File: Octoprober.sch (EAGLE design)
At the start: 135 parts, among them J1 10118193-0001LF, J2 26-60-4020, P1 TC33X-1, SW1 101-0134-EV, SW2 EVQ-Q2203W, SW3 EVQ-Q2203W, SW4 EVQ-Q2203W, SW5 EVQ-Q2203W, U1 P8X32A-M44, U10 MAX31855KASA+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

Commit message: Finished REV0.
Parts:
- BATT1: value 1042 -> (none); device PP_Connectors:LI-ION_18650_HOLDER1042 -> PP_Connectors:PH_1X02HEADER_PTH
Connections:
- net GND: now also BATT1.1; no longer BATT1.-
- net VBATT: now also BATT1.2; no longer BATT1.+
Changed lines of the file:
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@@
 <part name="C29" library="PP_Passives" deviceset="CAPACITOR_NON_POLAR" device="0402" value="0.1uF"/>
 <part name="C30" library="PP_Passives" deviceset="CAPACITOR_NON_POLAR" device="0402" value="0.01uF"/>
-<part name="BATT1" library="PP_Connectors" deviceset="LI-ION_18650_HOLDER" device="1042" value="1042"/>
 <part name="U5" library="PP_PowerIC" deviceset="BQ2407X" device="QFN-16" value="BQ24075RGTT"/>
 <part name="R14" library="PP_Passives" deviceset="RESISTOR" device="0402" value="10K"/>
@@
 <part name="D10" library="PP_Passives" deviceset="TVS_DIODE_DUAL" device="SOT-23" value="NUP2105LT1G"/>
 <part name="D11" library="PP_Passives" deviceset="TVS_DIODE_DUAL" device="SOT-23" value="NUP2105LT1G"/>
+<part name="BATT1" library="PP_Connectors" deviceset="PH_1X02" device="HEADER_PTH"/>
 </parts>
 <sheets>
@@
 <instance part="C29" gate="G$1" x="-223.52" y="-66.04"/>
 <instance part="C30" gate="G$1" x="-215.9" y="-66.04"/>
-<instance part="BATT1" gate="G$1" x="165.1" y="-12.7" rot="R90"/>
 <instance part="U5" gate="G$1" x="132.08" y="-2.54"/>
 <instance part="R14" gate="G$1" x="154.94" y="-17.78" rot="R270"/>
@@
 <instance part="D10" gate="G$1" x="-248.92" y="-50.8" rot="R270"/>
 <instance part="D11" gate="G$1" x="-248.92" y="-76.2" rot="R270"/>
+<instance part="BATT1" gate="G$1" x="162.56" y="-15.24" rot="R180"/>
 </instances>
 <busses>
@@
 </segment>
 <segment>
-<pinref part="BATT1" gate="G$1" pin="-"/>
-<wire x1="165.1" y1="-17.78" x2="165.1" y2="-33.02" width="0.1524" layer="91"/>
+<wire x1="165.1" y1="-15.24" x2="165.1" y2="-33.02" width="0.1524" layer="91"/>
 <pinref part="R14" gate="G$1" pin="2"/>
 <wire x1="154.94" y1="-22.86" x2="154.94" y2="-27.94" width="0.1524" layer="91"/>
@@
 <junction x="154.94" y="-27.94"/>
 <junction x="154.94" y="-33.02"/>
+<pinref part="BATT1" gate="G$1" pin="1"/>
+<wire x1="165.1" y1="-15.24" x2="162.56" y2="-15.24" width="0.1524" layer="91"/>
 </segment>
 <segment>
@@
 <net name="VBATT" class="0">
 <segment>
-<pinref part="BATT1" gate="G$1" pin="+"/>
-<wire x1="165.1" y1="-7.62" x2="165.1" y2="-2.54" width="0.1524" layer="91"/>
 <label x="152.4" y="-2.54" size="0.8128" layer="95" font="vector"/>
 <pinref part="U5" gate="G$1" pin="BAT"/>
@@
 <wire x1="172.72" y1="-2.54" x2="165.1" y2="-2.54" width="0.1524" layer="91"/>
 <junction x="165.1" y="-2.54"/>
-</segment>
-</net>
+<wire x1="165.1" y1="-2.54" x2="165.1" y2="-12.7" width="0.1524" layer="91"/>
+<pinref part="BATT1" gate="G$1" pin="2"/>
+<wire x1="165.1" y1="-12.7" x2="162.56" y2="-12.7" width="0.1524" layer="91"/>
+</segment>
+</net>

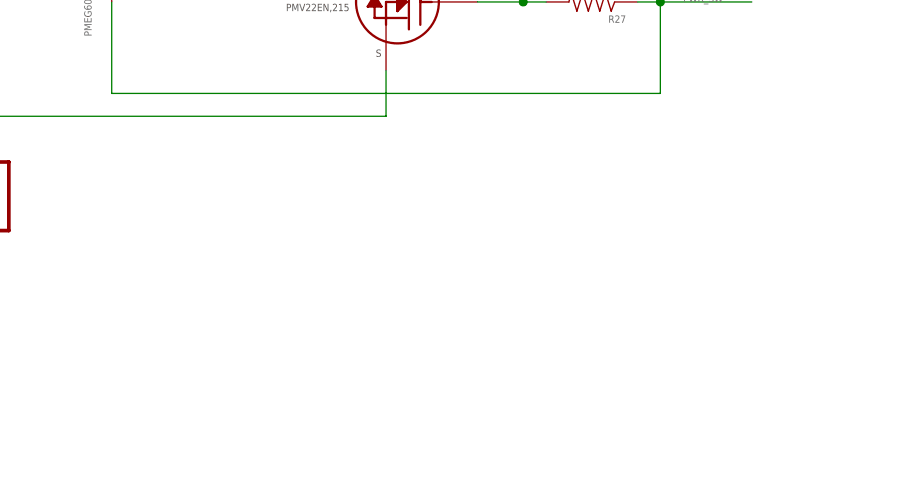
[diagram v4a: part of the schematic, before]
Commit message: Added ADC MCP3021 to monitor battery
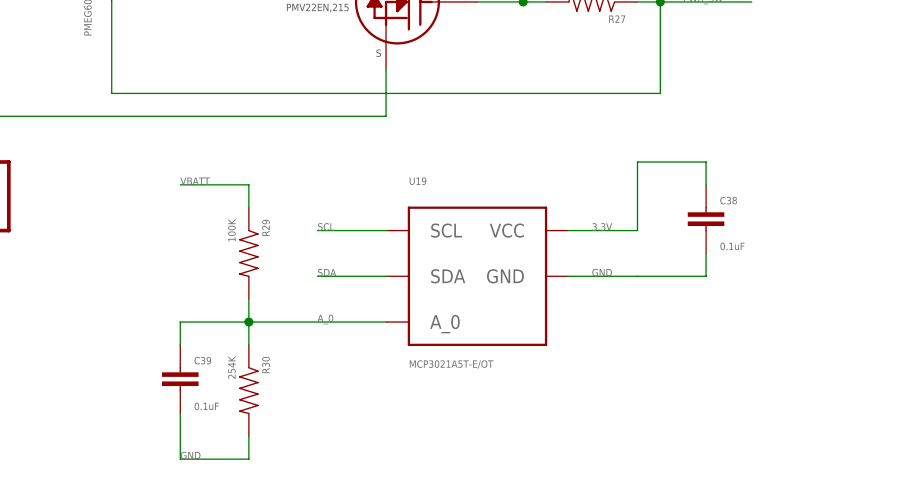
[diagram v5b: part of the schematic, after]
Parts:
- added C38, C39: 0.1uF, PP_Passives:CAPACITOR_NON_POLAR0402
- added R29: 100K, PP_Passives:RESISTOR0402
- added R30: 254K, PP_Passives:RESISTOR0402
- added U19: MCP3021A5T-E/OT, PP_DigitalIC:MCP3021SOT-23A
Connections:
- new net A_0: C39.1, R29.2, R30.1, U19.A_0
- net 3.3V: now also C38.1, U19.VCC
- net GND: now also C38.2, C39.2, R30.2, U19.GND
- net SCL: now also U19.SCL
- net SDA: now also U19.SDA
- net VBATT: now also R29.1
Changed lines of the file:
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@@
 <?xml version="1.0" encoding="utf-8"?>
 <!DOCTYPE eagle SYSTEM "eagle.dtd">
-<eagle version="6.5.0">
+<eagle version="6.3">
 <drawing>
 <settings>
@@
 <part name="D11" library="PP_Passives" deviceset="TVS_DIODE_DUAL" device="SOT-23" value="NUP2105LT1G"/>
 <part name="BATT1" library="PP_Connectors" deviceset="PH_1X02" device="HEADER_PTH"/>
+<part name="C38" library="PP_Passives" deviceset="CAPACITOR_NON_POLAR" device="0402" value="0.1uF"/>
+<part name="R29" library="PP_Passives" deviceset="RESISTOR" device="0402" value="100K"/>
+<part name="R30" library="PP_Passives" deviceset="RESISTOR" device="0402" value="254K"/>
+<part name="C39" library="PP_Passives" deviceset="CAPACITOR_NON_POLAR" device="0402" value="0.1uF"/>
+<part name="U19" library="PP_DigitalIC" deviceset="MCP3021" device="SOT-23A" value="MCP3021A5T-E/OT"/>
 </parts>
 <sheets>
@@
 <instance part="D11" gate="G$1" x="-248.92" y="-76.2" rot="R270"/>
 <instance part="BATT1" gate="G$1" x="162.56" y="-15.24" rot="R180"/>
+<instance part="C38" gate="G$1" x="144.78" y="-99.06"/>
+<instance part="R29" gate="G$1" x="93.98" y="-104.14" rot="R270"/>
+<instance part="R30" gate="G$1" x="93.98" y="-119.38" rot="R270"/>
+<instance part="C39" gate="G$1" x="86.36" y="-116.84"/>
+<instance part="U19" gate="G$1" x="119.38" y="-109.22"/>
 </instances>
 <busses>
@@
 <label x="-111.76" y="-119.38" size="0.8128" layer="95" font="vector"/>
 </segment>
+<segment>
+<wire x1="101.6" y1="-106.68" x2="109.22" y2="-106.68" width="0.1524" layer="91"/>
+<label x="101.6" y="-106.68" size="0.8128" layer="95" font="vector"/>
+<pinref part="U19" gate="G$1" pin="SDA"/>
+</segment>
 </net>
 <net name="SCL" class="0">
@@
 <wire x1="-104.14" y1="-114.3" x2="-114.3" y2="-114.3" width="0.1524" layer="91"/>
 <label x="-111.76" y="-114.3" size="0.8128" layer="95" font="vector"/>
+</segment>
+<segment>
+<wire x1="109.22" y1="-101.6" x2="101.6" y2="-101.6" width="0.1524" layer="91"/>
+<label x="101.6" y="-101.6" size="0.8128" layer="95" font="vector"/>
+<pinref part="U19" gate="G$1" pin="SCL"/>
 </segment>
 </net>
@@
 <pinref part="C37" gate="G$1" pin="2"/>
 <wire x1="-121.92" y1="-109.22" x2="-121.92" y2="-106.68" width="0.1524" layer="91"/>
+</segment>
+<segment>
+<wire x1="129.54" y1="-106.68" x2="137.16" y2="-106.68" width="0.1524" layer="91"/>
+<pinref part="C38" gate="G$1" pin="2"/>
+<wire x1="137.16" y1="-106.68" x2="144.78" y2="-106.68" width="0.1524" layer="91"/>
+<wire x1="144.78" y1="-106.68" x2="144.78" y2="-104.14" width="0.1524" layer="91"/>
+<label x="132.08" y="-106.68" size="0.8128" layer="95" font="vector"/>
+<pinref part="U19" gate="G$1" pin="GND"/>
+</segment>
+<segment>
+<pinref part="R30" gate="G$1" pin="2"/>
+<wire x1="93.98" y1="-124.46" x2="93.98" y2="-127" width="0.1524" layer="91"/>
+<wire x1="93.98" y1="-127" x2="86.36" y2="-127" width="0.1524" layer="91"/>
+<label x="86.36" y="-127" size="0.8128" layer="95" font="vector"/>
+<pinref part="C39" gate="G$1" pin="2"/>
+<wire x1="86.36" y1="-121.92" x2="86.36" y2="-127" width="0.1524" layer="91"/>
 </segment>
 </net>
@@
 <wire x1="-121.92" y1="-96.52" x2="-121.92" y2="-99.06" width="0.1524" layer="91"/>
 </segment>
+<segment>
+<wire x1="137.16" y1="-101.6" x2="129.54" y2="-101.6" width="0.1524" layer="91"/>
+<wire x1="137.16" y1="-101.6" x2="137.16" y2="-93.98" width="0.1524" layer="91"/>
+<pinref part="C38" gate="G$1" pin="1"/>
+<wire x1="137.16" y1="-93.98" x2="144.78" y2="-93.98" width="0.1524" layer="91"/>
+<wire x1="144.78" y1="-93.98" x2="144.78" y2="-96.52" width="0.1524" layer="91"/>
+<label x="132.08" y="-101.6" size="0.8128" layer="95" font="vector"/>
+<pinref part="U19" gate="G$1" pin="VCC"/>
+</segment>
 </net>
 <net name="SD_RW" class="0">
@@
 <pinref part="BATT1" gate="G$1" pin="2"/>
 <wire x1="165.1" y1="-12.7" x2="162.56" y2="-12.7" width="0.1524" layer="91"/>
+</segment>
+<segment>
+<pinref part="R29" gate="G$1" pin="1"/>
+<wire x1="93.98" y1="-99.06" x2="93.98" y2="-96.52" width="0.1524" layer="91"/>
+<wire x1="93.98" y1="-96.52" x2="86.36" y2="-96.52" width="0.1524" layer="91"/>
+<label x="86.36" y="-96.52" size="0.8128" layer="95" font="vector"/>
 </segment>
 </net>
@@
 </segment>
 </net>
+<net name="A_0" class="0">
+<segment>
+<pinref part="R29" gate="G$1" pin="2"/>
+<wire x1="109.22" y1="-111.76" x2="93.98" y2="-111.76" width="0.1524" layer="91"/>
+<wire x1="93.98" y1="-111.76" x2="93.98" y2="-109.22" width="0.1524" layer="91"/>
+<pinref part="R30" gate="G$1" pin="1"/>
+<wire x1="93.98" y1="-111.76" x2="93.98" y2="-114.3" width="0.1524" layer="91"/>
+<junction x="93.98" y="-111.76"/>
+<label x="101.6" y="-111.76" size="0.8128" layer="95" font="vector"/>
+<pinref part="C39" gate="G$1" pin="1"/>
+<wire x1="93.98" y1="-111.76" x2="86.36" y2="-111.76" width="0.1524" layer="91"/>
+<wire x1="86.36" y1="-111.76" x2="86.36" y2="-114.3" width="0.1524" layer="91"/>
+<pinref part="U19" gate="G$1" pin="A_0"/>
+</segment>
+</net>

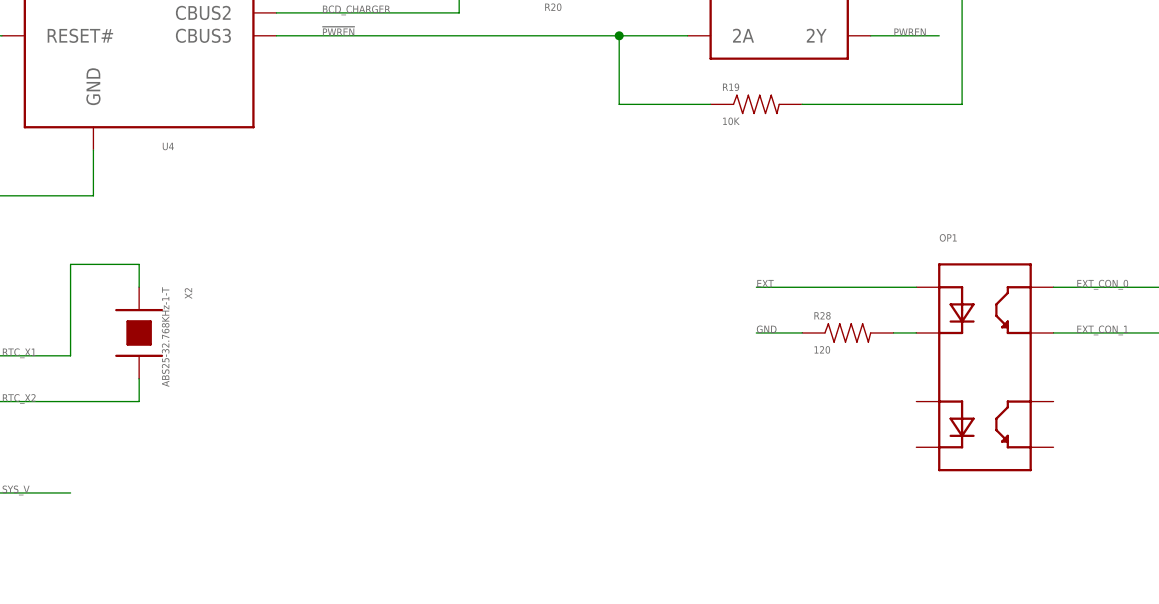
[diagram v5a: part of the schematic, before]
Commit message: Added part values and created BOM.txt
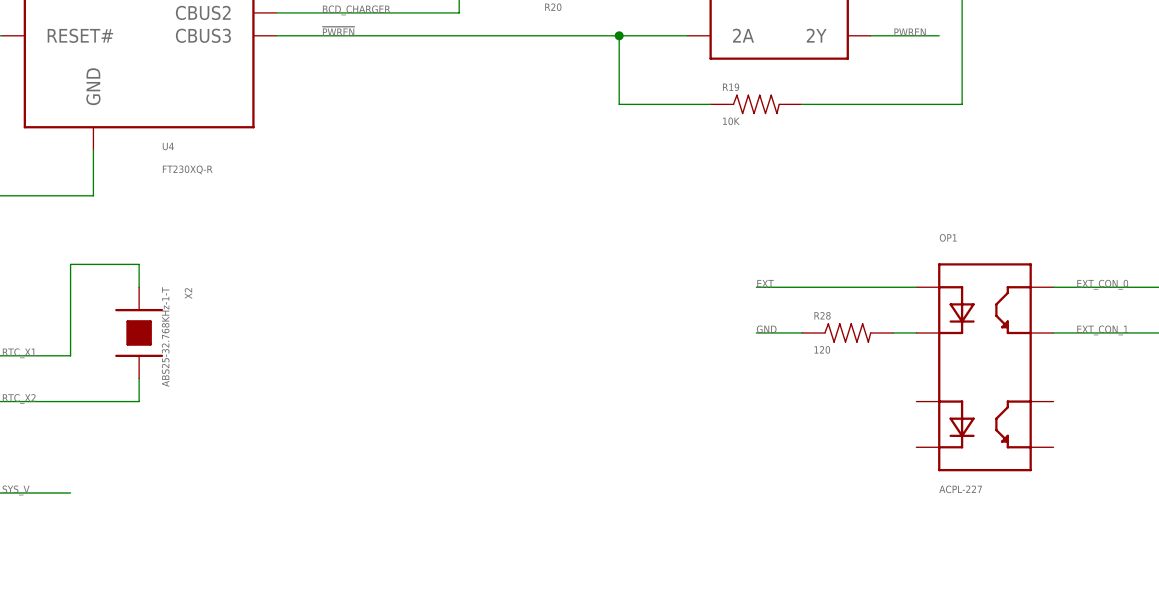
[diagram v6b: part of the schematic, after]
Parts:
- OP1: value (none) -> ACPL-227
- U4: value (none) -> FT230XQ-R
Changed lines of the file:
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@@
 <?xml version="1.0" encoding="utf-8"?>
 <!DOCTYPE eagle SYSTEM "eagle.dtd">
-<eagle version="6.3">
+<eagle version="6.5.0">
 <drawing>
 <settings>
@@
 <part name="J1" library="PP_Connectors" deviceset="USB" device="10118193-0001LF" value="10118193-0001LF"/>
 <part name="L1" library="PP_Passives" deviceset="RESISTOR" device="0603" value="MI0603K300R-10"/>
-<part name="U4" library="PP_DigitalIC" deviceset="FT230X" device="QFN-16"/>
+<part name="U4" library="PP_DigitalIC" deviceset="FT230X" device="QFN-16" value="FT230XQ-R"/>
 <part name="C11" library="PP_Passives" deviceset="CAPACITOR_NON_POLAR" device="0402" value="0.1uF"/>
 <part name="R10" library="PP_Passives" deviceset="RESISTOR" device="0402" value="22"/>
@@
 <part name="U$2" library="PP_Aesthetics" deviceset="OCTOPROBER_LOGO" device="NORMAL"/>
 <part name="J2" library="PP_Connectors" deviceset="PH_1X02" device="MOLEX_26-61-4020" value="26-60-4020"/>
-<part name="OP1" library="PP_DigitalIC" deviceset="ACPL-227" device="SOIC-8"/>
+<part name="OP1" library="PP_DigitalIC" deviceset="ACPL-227" device="SOIC-8" value="ACPL-227"/>
 <part name="R28" library="PP_Passives" deviceset="RESISTOR" device="0402" value="120"/>
 <part name="TC1" library="PP_Connectors" deviceset="PH_1X02" device="HEADER_PTH"/>

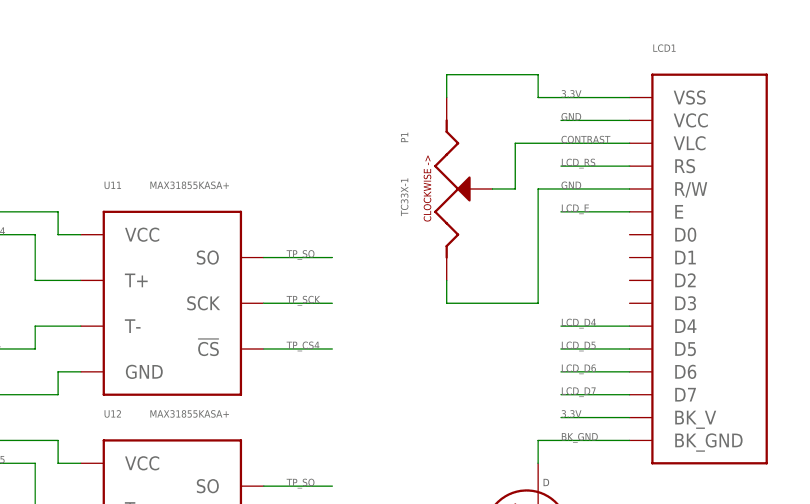
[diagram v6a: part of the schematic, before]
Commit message: Fixed some part numbers
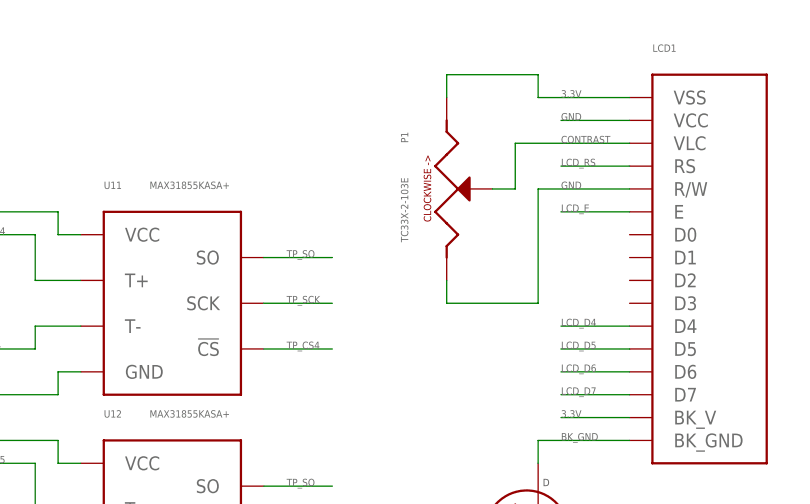
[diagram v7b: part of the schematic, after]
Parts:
- P1: value TC33X-1 -> TC33X-2-103E
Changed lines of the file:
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@@
 </part>
 <part name="LCD1" library="PP_Displays" deviceset="HD44780_LCD" device="1602_COUNTERSINK"/>
-<part name="P1" library="PP_Passives" deviceset="TC33X-1" device="TC33X-1" value="TC33X-1"/>
+<part name="P1" library="PP_Passives" deviceset="TC33X-1" device="TC33X-1" value="TC33X-2-103E"/>
 <part name="U7" library="PP_Sensors" deviceset="MAX31855" device="SO-8" value="MAX31855KASA+"/>
 <part name="C15" library="PP_Passives" deviceset="CAPACITOR_NON_POLAR" device="0402" value="0.1uF"/>

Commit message: Finished BOM...I hope.
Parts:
- BATT1: value (none) -> MIKROE-1120
- TC1, TC2, TC3, TC4, TC5, TC6, TC7, TC8: value (none) -> 282834-2
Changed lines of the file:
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@@
 <part name="OP1" library="PP_DigitalIC" deviceset="ACPL-227" device="SOIC-8" value="ACPL-227"/>
 <part name="R28" library="PP_Passives" deviceset="RESISTOR" device="0402" value="120"/>
-<part name="TC1" library="PP_Connectors" deviceset="PH_1X02" device="HEADER_PTH"/>
-<part name="TC2" library="PP_Connectors" deviceset="PH_1X02" device="HEADER_PTH"/>
-<part name="TC3" library="PP_Connectors" deviceset="PH_1X02" device="HEADER_PTH"/>
-<part name="TC4" library="PP_Connectors" deviceset="PH_1X02" device="HEADER_PTH"/>
-<part name="TC5" library="PP_Connectors" deviceset="PH_1X02" device="HEADER_PTH"/>
-<part name="TC6" library="PP_Connectors" deviceset="PH_1X02" device="HEADER_PTH"/>
-<part name="TC7" library="PP_Connectors" deviceset="PH_1X02" device="HEADER_PTH"/>
-<part name="TC8" library="PP_Connectors" deviceset="PH_1X02" device="HEADER_PTH"/>
+<part name="TC1" library="PP_Connectors" deviceset="PH_1X02" device="HEADER_PTH" value="282834-2"/>
+<part name="TC2" library="PP_Connectors" deviceset="PH_1X02" device="HEADER_PTH" value="282834-2"/>
+<part name="TC3" library="PP_Connectors" deviceset="PH_1X02" device="HEADER_PTH" value="282834-2"/>
+<part name="TC4" library="PP_Connectors" deviceset="PH_1X02" device="HEADER_PTH" value="282834-2"/>
+<part name="TC5" library="PP_Connectors" deviceset="PH_1X02" device="HEADER_PTH" value="282834-2"/>
+<part name="TC6" library="PP_Connectors" deviceset="PH_1X02" device="HEADER_PTH" value="282834-2"/>
+<part name="TC7" library="PP_Connectors" deviceset="PH_1X02" device="HEADER_PTH" value="282834-2"/>
+<part name="TC8" library="PP_Connectors" deviceset="PH_1X02" device="HEADER_PTH" value="282834-2"/>
 <part name="U18" library="PP_DigitalIC" deviceset="DS1340" device="SOIC-8" value="DS1340Z-33+"/>
 <part name="C37" library="PP_Passives" deviceset="CAPACITOR_NON_POLAR" device="0402" value="0.1uF"/>
@@
 <part name="D10" library="PP_Passives" deviceset="TVS_DIODE_DUAL" device="SOT-23" value="NUP2105LT1G"/>
 <part name="D11" library="PP_Passives" deviceset="TVS_DIODE_DUAL" device="SOT-23" value="NUP2105LT1G"/>
-<part name="BATT1" library="PP_Connectors" deviceset="PH_1X02" device="HEADER_PTH"/>
+<part name="BATT1" library="PP_Connectors" deviceset="PH_1X02" device="HEADER_PTH" value="MIKROE-1120"/>
 <part name="C38" library="PP_Passives" deviceset="CAPACITOR_NON_POLAR" device="0402" value="0.1uF"/>
 <part name="R29" library="PP_Passives" deviceset="RESISTOR" device="0402" value="100K"/>
